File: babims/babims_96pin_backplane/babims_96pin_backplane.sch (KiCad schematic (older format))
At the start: 2 parts

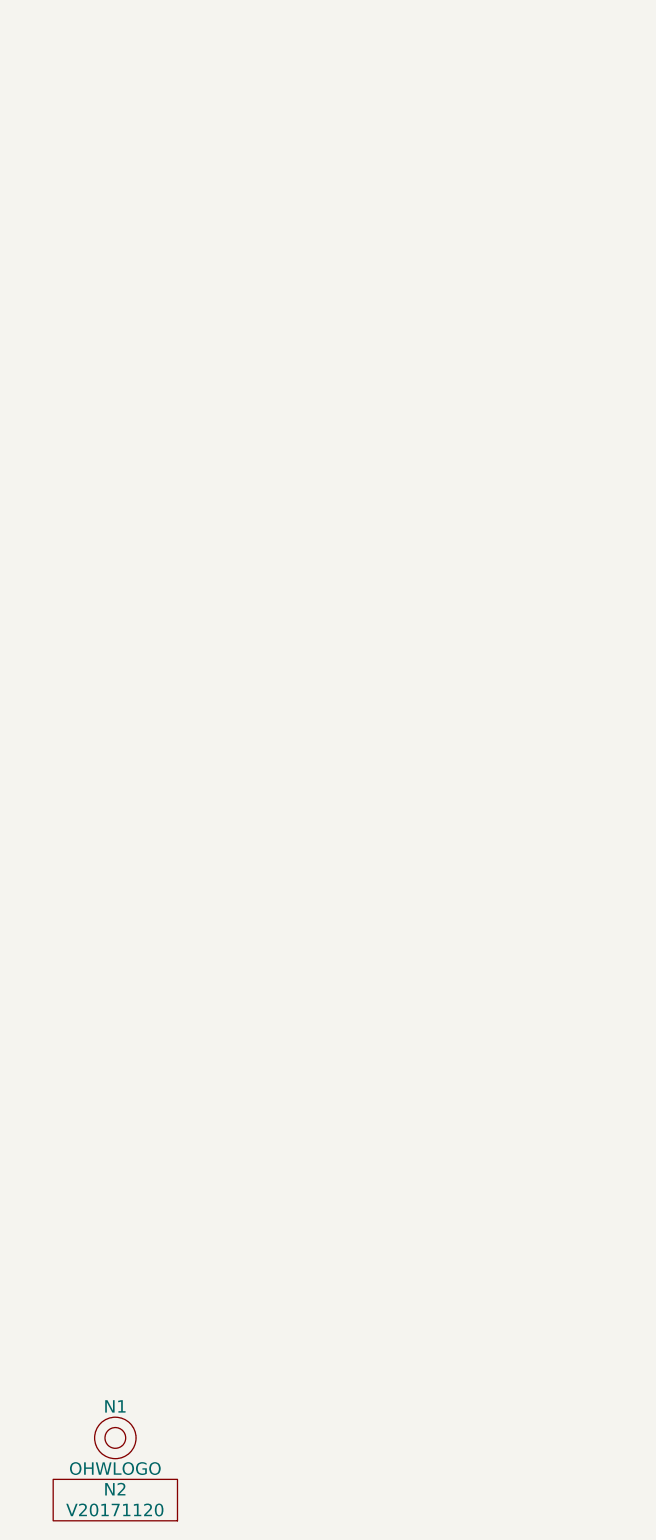
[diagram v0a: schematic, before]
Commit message: * first definition of the connection nets
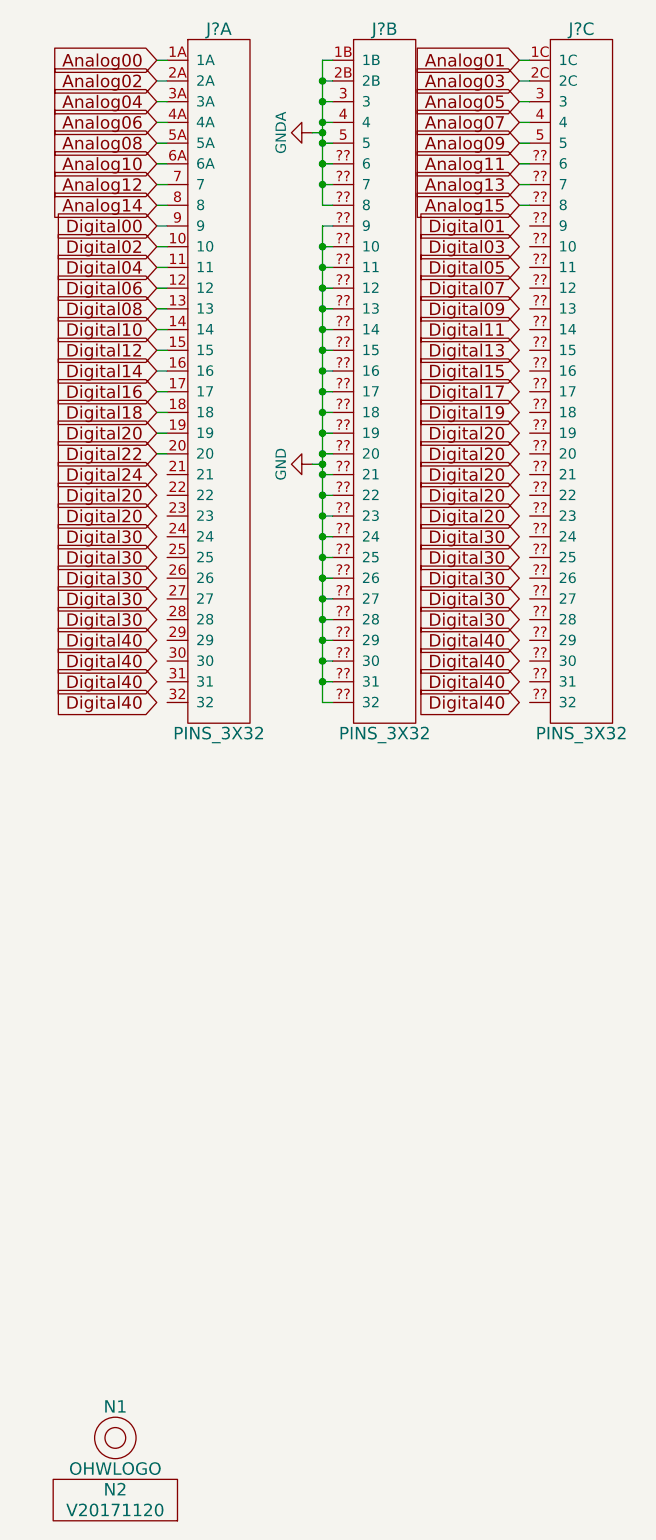
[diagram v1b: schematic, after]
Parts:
- added J? (x3): PINS_3X32, symbol PINS_3X32
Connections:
- new net Analog00: J?.1A
- new net Analog01: J?.1C
- new net Analog02: J?.2A
- new net Analog03: J?.2C
- new net Analog04: J?.3A
- new net Analog05: J?.3
- new net Analog06: J?.4A
- new net Analog07: J?.4
- new net Analog08: J?.5A
- new net Analog09: J?.5
- new net Analog10: J?.6A
- new net Analog11: J?.?? (9)
- new net Analog12: J?.7
- new net Analog13: J?.?? (9)
- new net Analog14: J?.8
- new net Analog15: J?.?? (9)
- new net Digital00: J?.9
- new net Digital02: J?.10
- new net Digital04: J?.11
- new net Digital06: J?.12
- new net Digital08: J?.13
- new net Digital10: J?.14
- new net Digital12: J?.15
- new net Digital14: J?.16
- new net Digital16: J?.17
- new net Digital18: J?.18
- new net Digital20: J?.19
- new net Digital22: J?.20
- new net GND: J?.?? (9)
- new net GNDA: J?.1B, J?.2B, J?.3, J?.4, J?.5, J?.?? (9)
